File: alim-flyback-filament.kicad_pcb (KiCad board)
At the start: 2 copper layers, 70 x 55 mm, 47 parts, among them Q1 IPD050N10N5, Q2 IPD050N10N5, T1 MSD1514-103ME, U1 UCC27517, U2 UCC27517, U3 ISO7710, U4 ISO7710, U5 DPC817

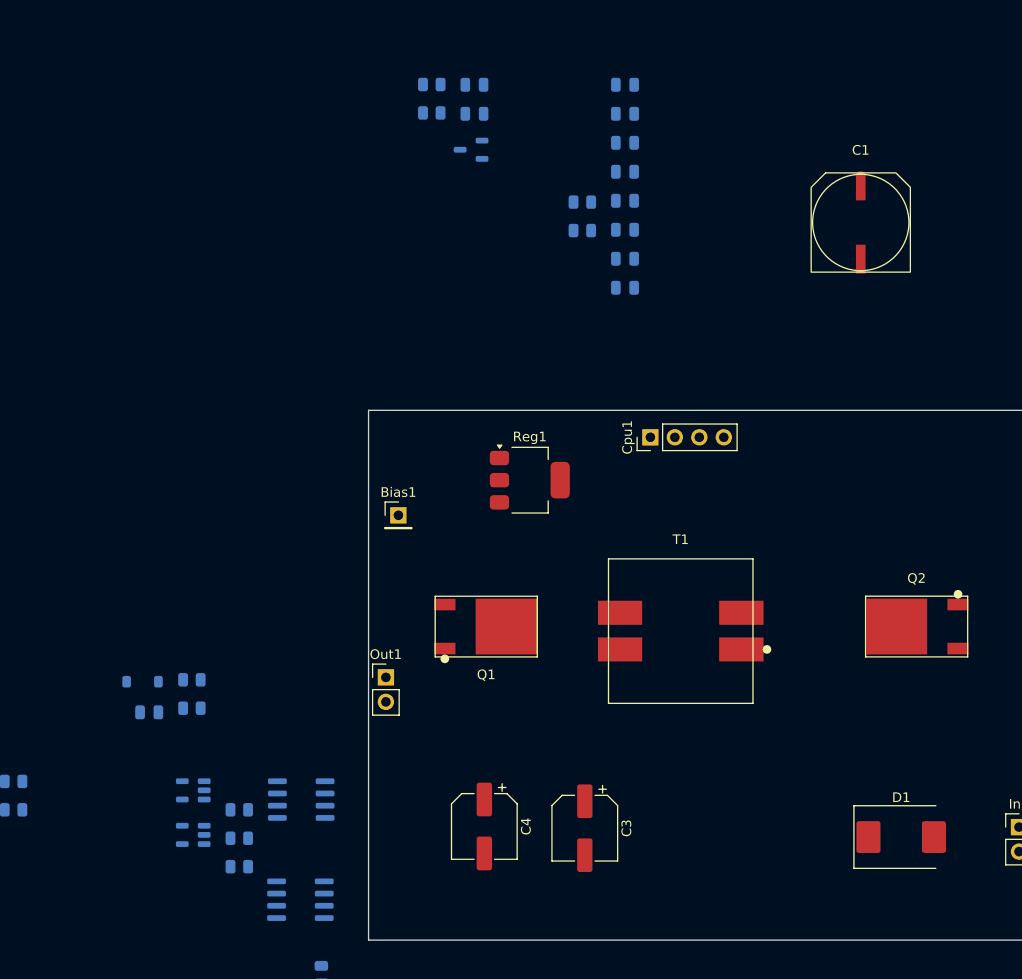
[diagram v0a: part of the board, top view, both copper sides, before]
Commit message: Secondaire ISO7710+UCC27517 conservé, ajout retour Vout isolé AMC0311S, modèles 3D
- D2 (bootstrap) remplacé par BAT54C (cathode commune) pour compatibilité pinout
- AMC0311S (U7) ajouté : retour de mesure Vout isolé vers le connecteur C2000
- Connecteur Cpu1 étendu à 8 broches (signaux + masses)
- Correction pastilles Gate/Source sur l'empreinte custom TO-252 (pin1/pin3 inversées)
- Modèles 3D attachés aux empreintes custom (TO-252, MSD1514, A786MW V-chip)
- Image de rendu 3D ajoutée au README

Co-Authored-By: Claude Sonnet 5 <noreply@anthropic.com>
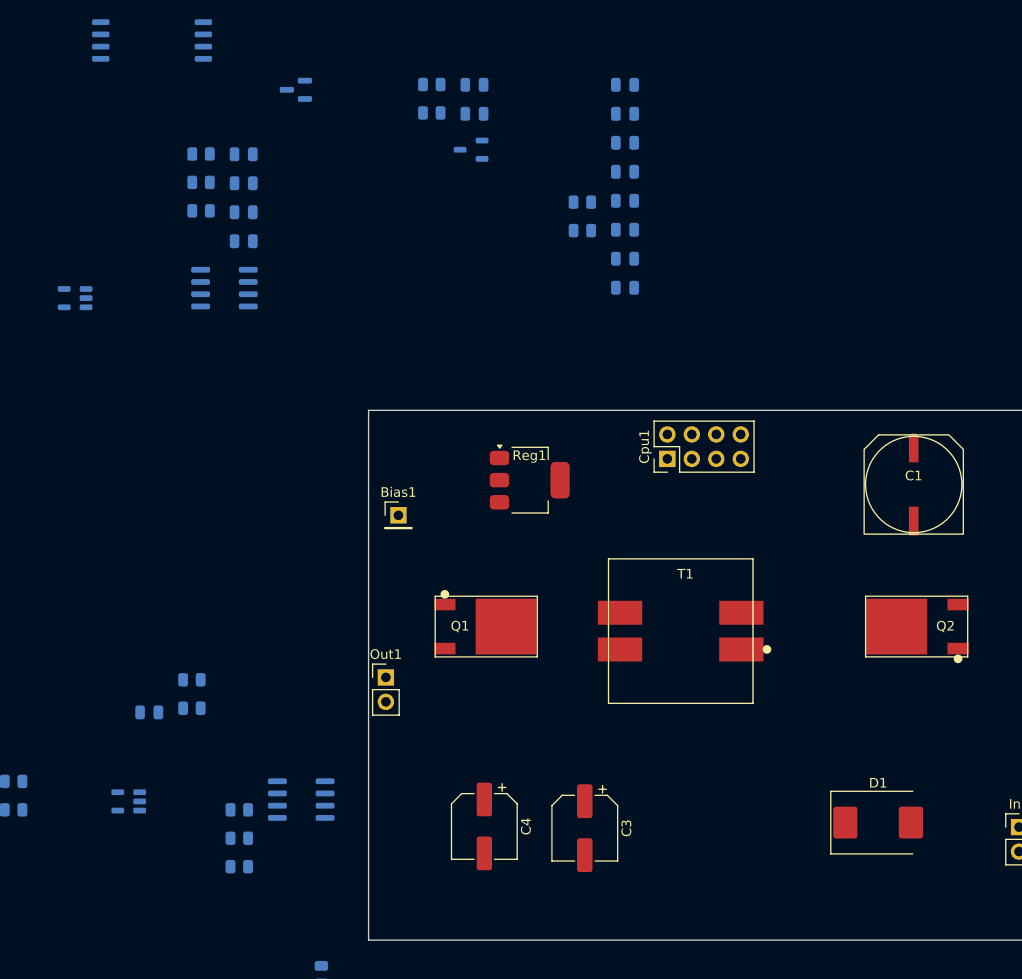
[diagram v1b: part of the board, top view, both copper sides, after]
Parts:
- added C23: 100p, Capacitor_SMD:C_0805_2012Metric, B.Cu at (87.0, 53.4)
- added C24: 1n, Capacitor_SMD:C_0805_2012Metric, B.Cu at (87.0, 56.4)
- added C27: 100n, Capacitor_SMD:C_0805_2012Metric, B.Cu at (87.0, 59.4)
- added C28: 100n, Capacitor_SMD:C_0805_2012Metric, B.Cu at (87.0, 62.4)
- added R13: 51k, Resistor_SMD:R_0805_2012Metric, B.Cu at (82.6, 53.4)
- added R14: 10k, Resistor_SMD:R_0805_2012Metric, B.Cu at (82.6, 56.3)
- added R15: 100, Resistor_SMD:R_0805_2012Metric, B.Cu at (82.6, 59.3)
- added U7: AMC0311S, Package_SO:SOIC-8_7.5x5.85mm_P1.27mm, B.Cu at (77.5, 41.6)
- Cpu1: value CTRL -> CTRL_C2000; footprint Connector_PinHeader_2.54mm:PinHeader_1x04_P2.54mm_Vertical -> Connector_PinHeader_2.54mm:PinHeader_2x04_P2.54mm_Vertical
- D2: value BAT54 -> BAT54C; footprint Diode_SMD:D_SOD-123 -> Package_TO_SOT_SMD:SOT-23
- moved U4 64.0 mm to (85.0, 67.3)
- moved D2 63.5 mm to (92.5, 46.7)
- moved U2 57.1 mm to (69.5, 68.3)
- moved C1 27.8 mm to (156.6, 87.7)
- moved U1 6.80 mm to (75.1, 120.6)
- moved Cpu1 2.85 mm to (131.0, 85.0)
- moved D1 2.83 mm to (152.9, 122.8)
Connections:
- net Net-(U2-OUT) renamed SEC_GATE_DRV
- Cpu1 pad 2: EN_PRI_IN -> GND
- Cpu1 pad 3: PWM_SEC_IN -> EN_PRI_IN
- D1 pad 1: GND -> SW_PRI
- D1 pad 2: SW_PRI -> GND
- D2 pad 2: VBOOT -> VOUT_P

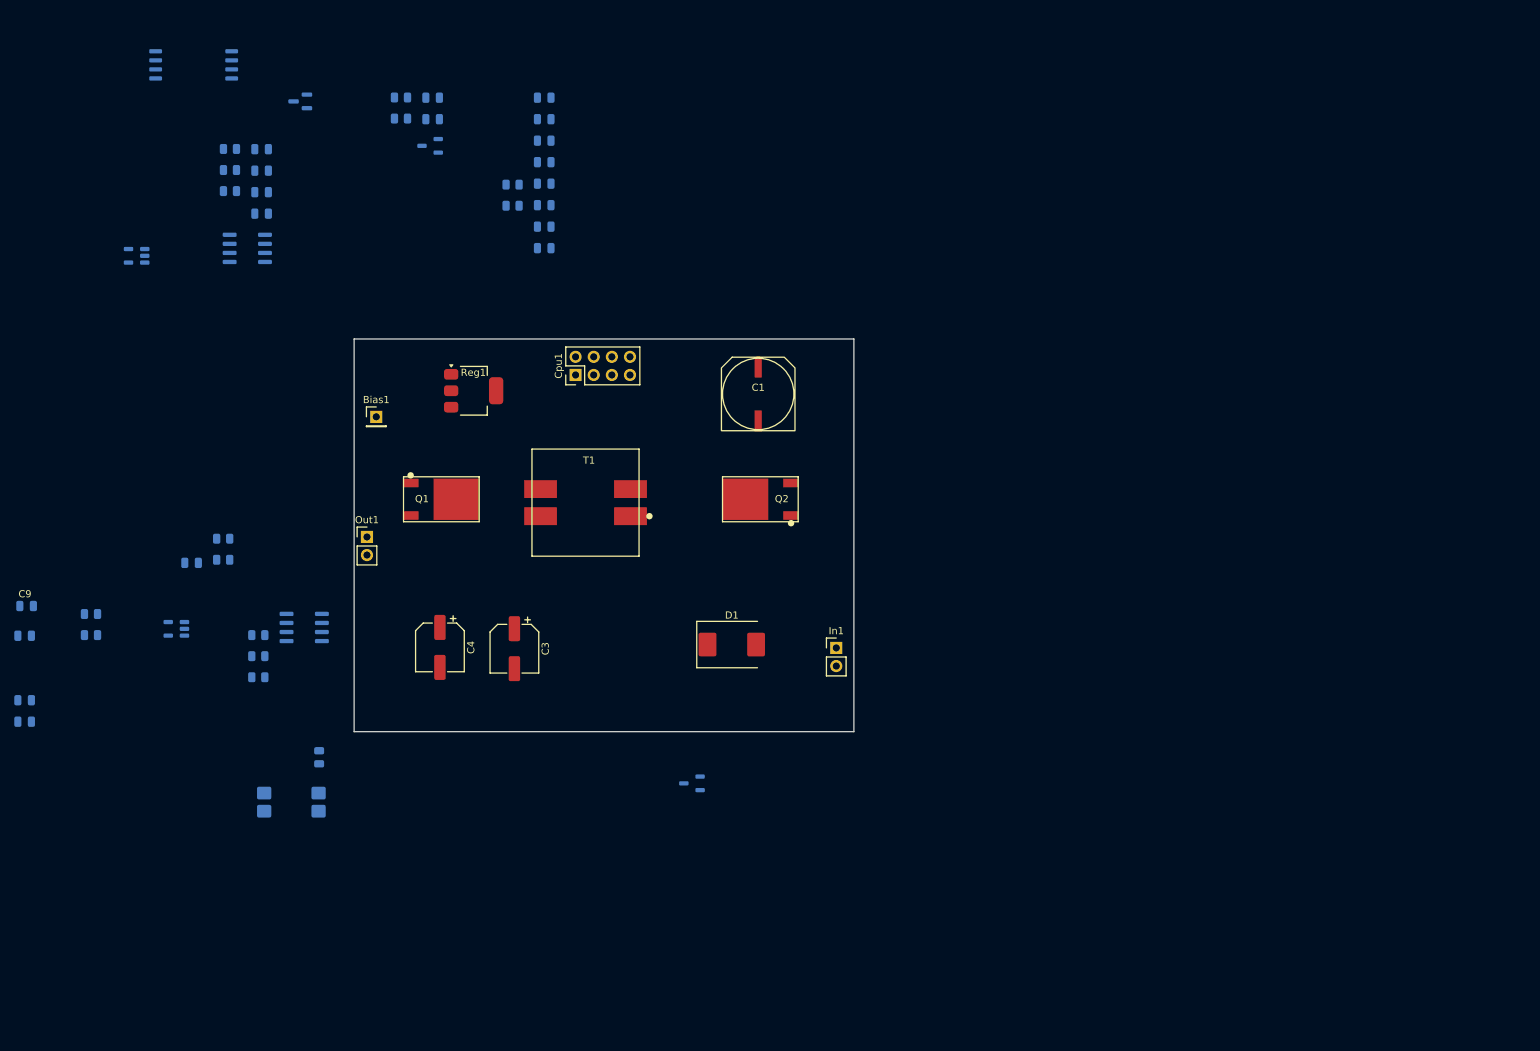
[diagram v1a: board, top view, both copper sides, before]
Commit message: Isolation C2000 réelle (GND_CTRL/3V3_CTRL) + feuille Polarisation (HV_BIAS actif 0-90V)
- U3/U4/U5/U7/U8/U9 migrés côté contrôle vers GND_CTRL/3V3_CTRL (isolation
  du C2000 réellement effective, plus seulement nominale)
- Connecteurs CpuOut/CpuIn agrandis 2x04→2x08 (16 broches), marge pour
  futurs signaux et compatibilité avec d'autres cartes
- Nouvelle feuille polarisation.kicad_sch : pilotage actif de HV_BIAS
  (point de polarisation du secondaire flottant) depuis une alimentation
  400V externe — source de courant 300µA (BSS127I+MMBT2222), MOSFET
  variable BSS127I piloté par PWM isolé (ISO7710), protection TVS +
  pull-up grille, retour mesure isolé (AMC0311R)
- Nouveaux symboles custom BSS127I/MMBT2222, empreinte SOIC_DWV partagée
  par les amplis isolés de la famille AMC03x1R/AMC03x2R

Co-Authored-By: Claude Sonnet 5 <noreply@anthropic.com>
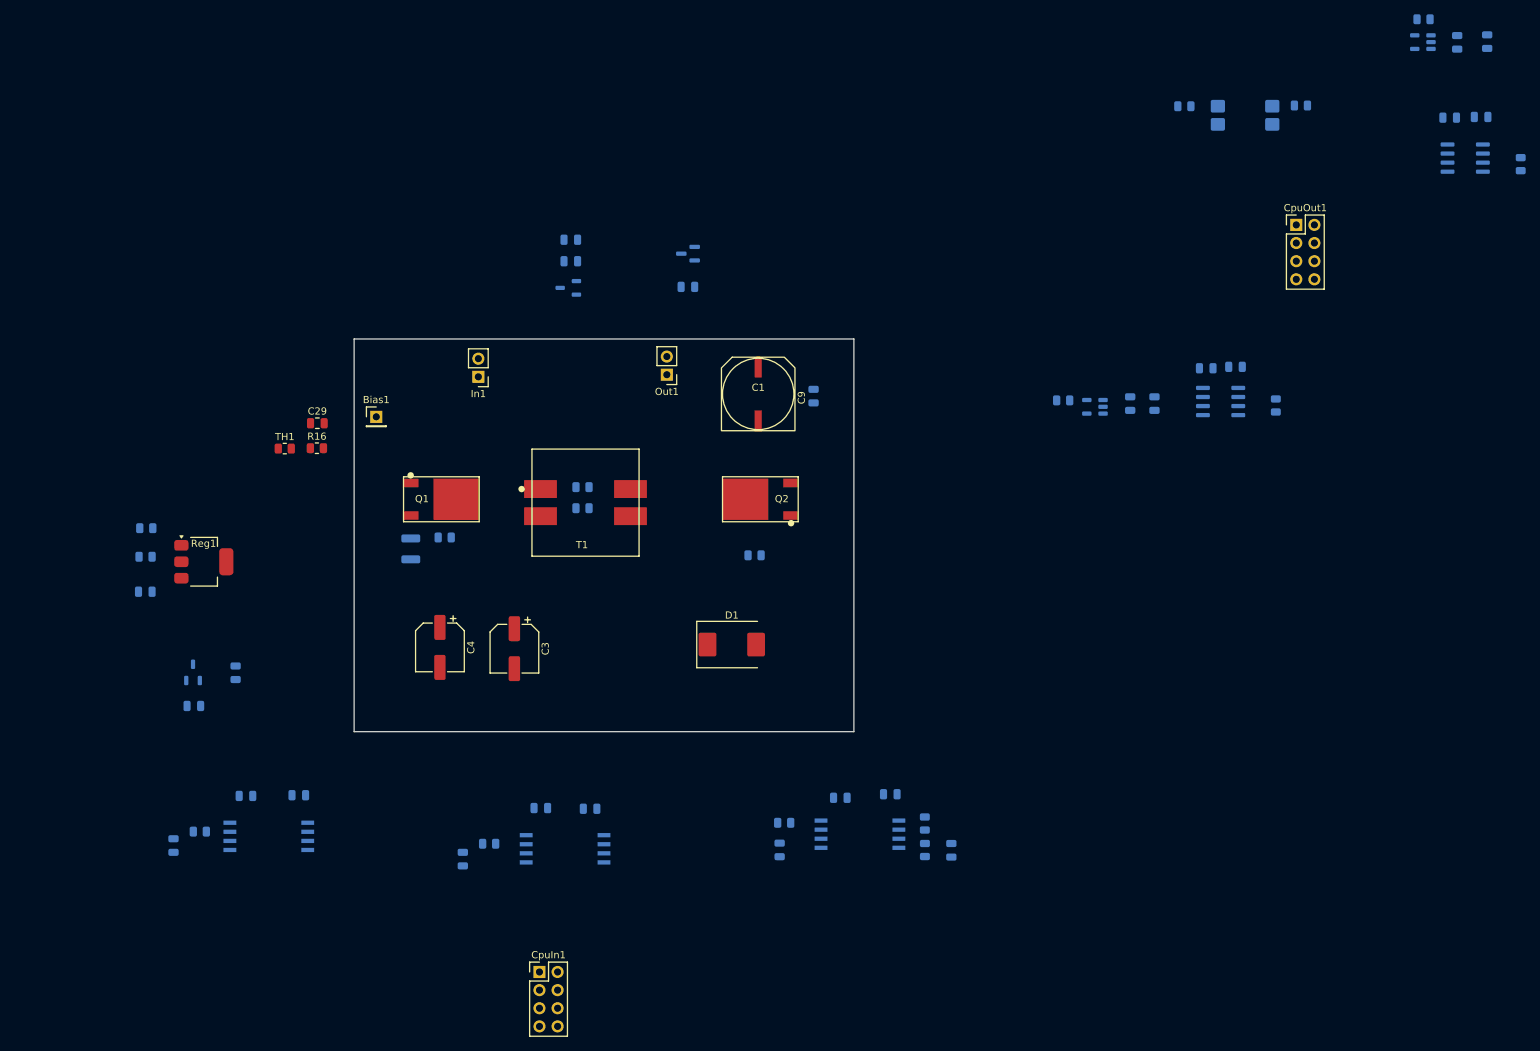
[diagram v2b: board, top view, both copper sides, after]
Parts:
- removed Cpu1: CTRL_C2000, Connector_PinHeader_2.54mm:PinHeader_2x04_P2.54mm_Vertical
- added C25: 100n, Capacitor_SMD:C_0805_2012Metric, B.Cu at (92.2, 143.9)
- added C26: 100n, Capacitor_SMD:C_0805_2012Metric, B.Cu at (84.8, 144.0)
- added C29: 100p, Capacitor_SMD:C_0805_2012Metric, F.Cu at (94.8, 91.8)
- added C30: 1n, Capacitor_SMD:C_0805_2012Metric, B.Cu at (74.7, 150.9)
- added C31: 100n, Capacitor_SMD:C_0805_2012Metric, B.Cu at (133.1, 145.8)
- added C32: 100n, Capacitor_SMD:C_0805_2012Metric, B.Cu at (126.2, 145.7)
- added C33: 1n, Capacitor_SMD:C_0805_2012Metric, B.Cu at (115.2, 152.8)
- added CpuIn1: CTRL_C2000_IN, Connector_PinHeader_2.54mm:PinHeader_2x04_P2.54mm_Vertical, F.Cu at (126.0, 168.7)
- added CpuOut1: CTRL_C2000_OUT, Connector_PinHeader_2.54mm:PinHeader_2x04_P2.54mm_Vertical, F.Cu at (232.0, 64.0)
- added R16: 10k, Resistor_SMD:R_0805_2012Metric, F.Cu at (94.8, 95.3)
- added R17: 100, Resistor_SMD:R_0805_2012Metric, B.Cu at (78.4, 149.0)
- added R18: 100, Resistor_SMD:R_0805_2012Metric, B.Cu at (118.9, 150.7)
- added R19: 7m5, Resistor_SMD:R_1210_3225Metric, B.Cu at (107.9, 109.4)
- added TH1: 10k_B4000, Resistor_SMD:R_0805_2012Metric, F.Cu at (90.3, 95.3)
- added U8: AMC0311R, SOIC_DWV:SOIC-8_DWV_5.85x11.5mm_P1.27mm, B.Cu at (88.0, 149.7)
- added U9: AMC0302R, SOIC_DWV:SOIC-8_DWV_5.85x11.5mm_P1.27mm, B.Cu at (129.6, 151.4)
- U7: value AMC0311S -> AMC0311R; footprint Package_SO:SOIC-8_7.5x5.85mm_P1.27mm -> SOIC_DWV:SOIC-8_DWV_5.85x11.5mm_P1.27mm
- moved U1 193.0 mm to (249.7, 38.4)
- moved R5 189.8 mm to (263.4, 55.5), turned to -90 degrees
- moved U3 175.4 mm to (255.6, 54.7)
- moved R3 165.1 mm to (232.6, 47.3), turned to 180 degrees
- moved U5 164.6 mm to (224.8, 48.7)
- moved R4 149.4 mm to (216.3, 47.4), turned to 0 degrees
- moved R6 147.5 mm to (229.1, 89.3), turned to -90 degrees
- moved U7 142.6 mm to (170.8, 149.4)
- moved U4 138.0 mm to (221.4, 88.8)
- moved C23 137.8 mm to (183.7, 151.6), turned to -90 degrees
- moved R14 136.2 mm to (179.9, 151.6), turned to -90 degrees
- moved U2 135.9 mm to (203.8, 89.5)
- moved R13 135.6 mm to (179.9, 147.9), turned to -90 degrees
- moved C21 134.6 mm to (258.7, 38.4), turned to -90 degrees
- moved C27 134.6 mm to (219.3, 84.1), turned to 0 degrees
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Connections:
- net EN_PRI_IN_R renamed Net-(R3-Pad2)
- net LM317_ADJ renamed Net-(Reg1-ADJ)
- net SEC_GATE_DRV renamed Net-(U2-OUT)
- C15 pad 1: RAIL_3V3_PRI -> 3V3_CTRL
- C15 pad 2: GND -> GND_CTRL
- C17 pad 1: RAIL_3V3_PRI -> 3V3_CTRL
- C17 pad 2: GND -> GND_CTRL
- C18 pad 2: GND -> VOUT_N
- C20 pad 2: GND -> VOUT_N
- C22 pad 2: GND -> VOUT_N
- C24 pad 2: GND -> GND_CTRL
- C28 pad 1: RAIL_3V3_PRI -> 3V3_CTRL
- C28 pad 2: GND -> GND_CTRL
- Q1 pad 3: GND -> ISENSE_P
- R5 pad 2: GND -> GND_CTRL
- R6 pad 2: GND -> GND_CTRL
- U3 pad 1: RAIL_3V3_PRI -> 3V3_CTRL
- U3 pad 3: RAIL_3V3_PRI -> 3V3_CTRL
- U3 pad 4: GND -> GND_CTRL
- U4 pad 1: RAIL_3V3_PRI -> 3V3_CTRL
- U4 pad 4: GND -> GND_CTRL
- U5 pad 2: GND -> GND_CTRL
- U7 pad 5: GND -> GND_CTRL
- U7 pad 6: GND -> GND_CTRL
- U7 pad 8: RAIL_3V3_PRI -> 3V3_CTRL
